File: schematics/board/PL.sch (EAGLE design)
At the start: 28 parts, among them IC2 STM32F103C8T, Q5 8MHz

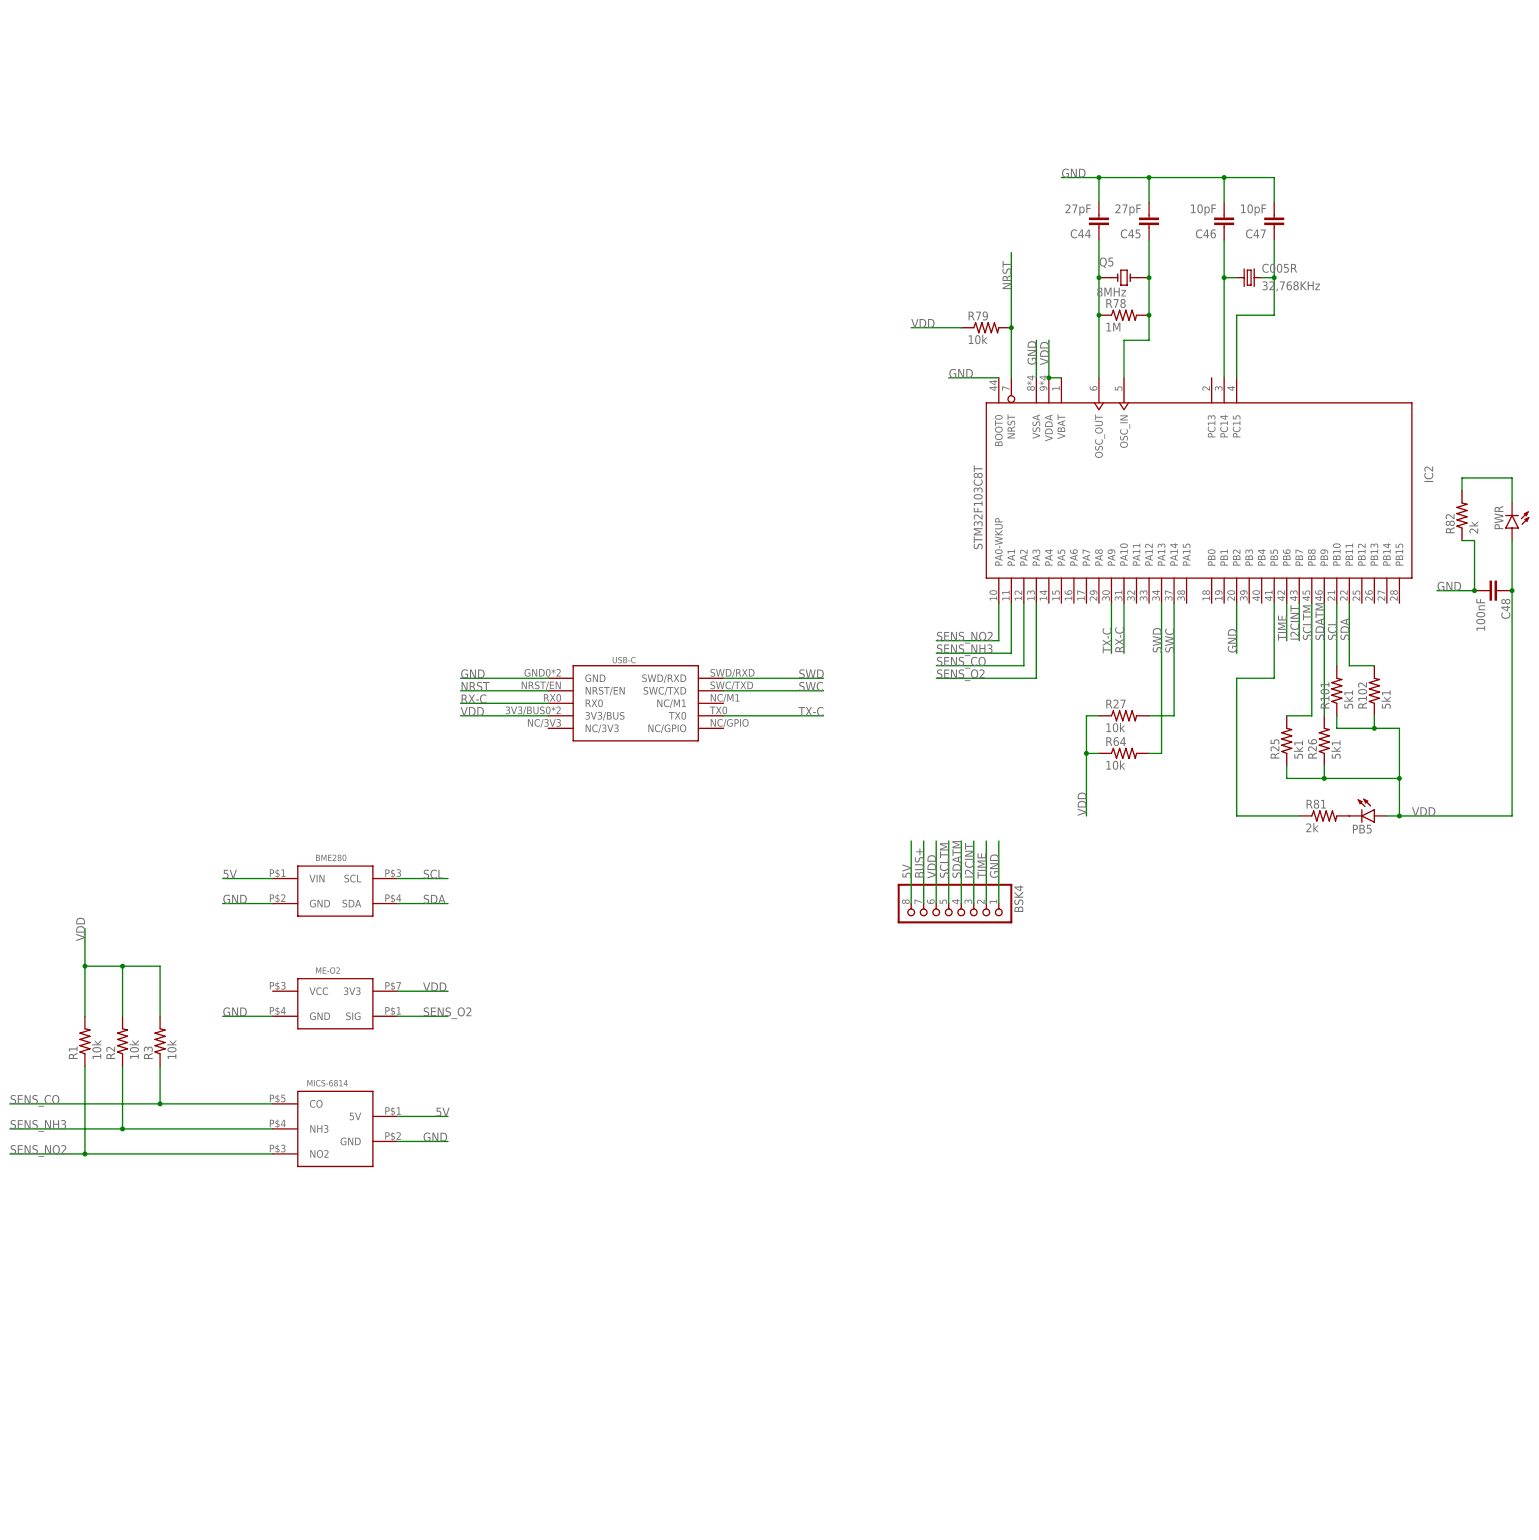
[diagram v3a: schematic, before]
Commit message: На плату полезной нагрузки добавлены управляемые резисторы для управления балансирующими сопротивлениями для газового датчика
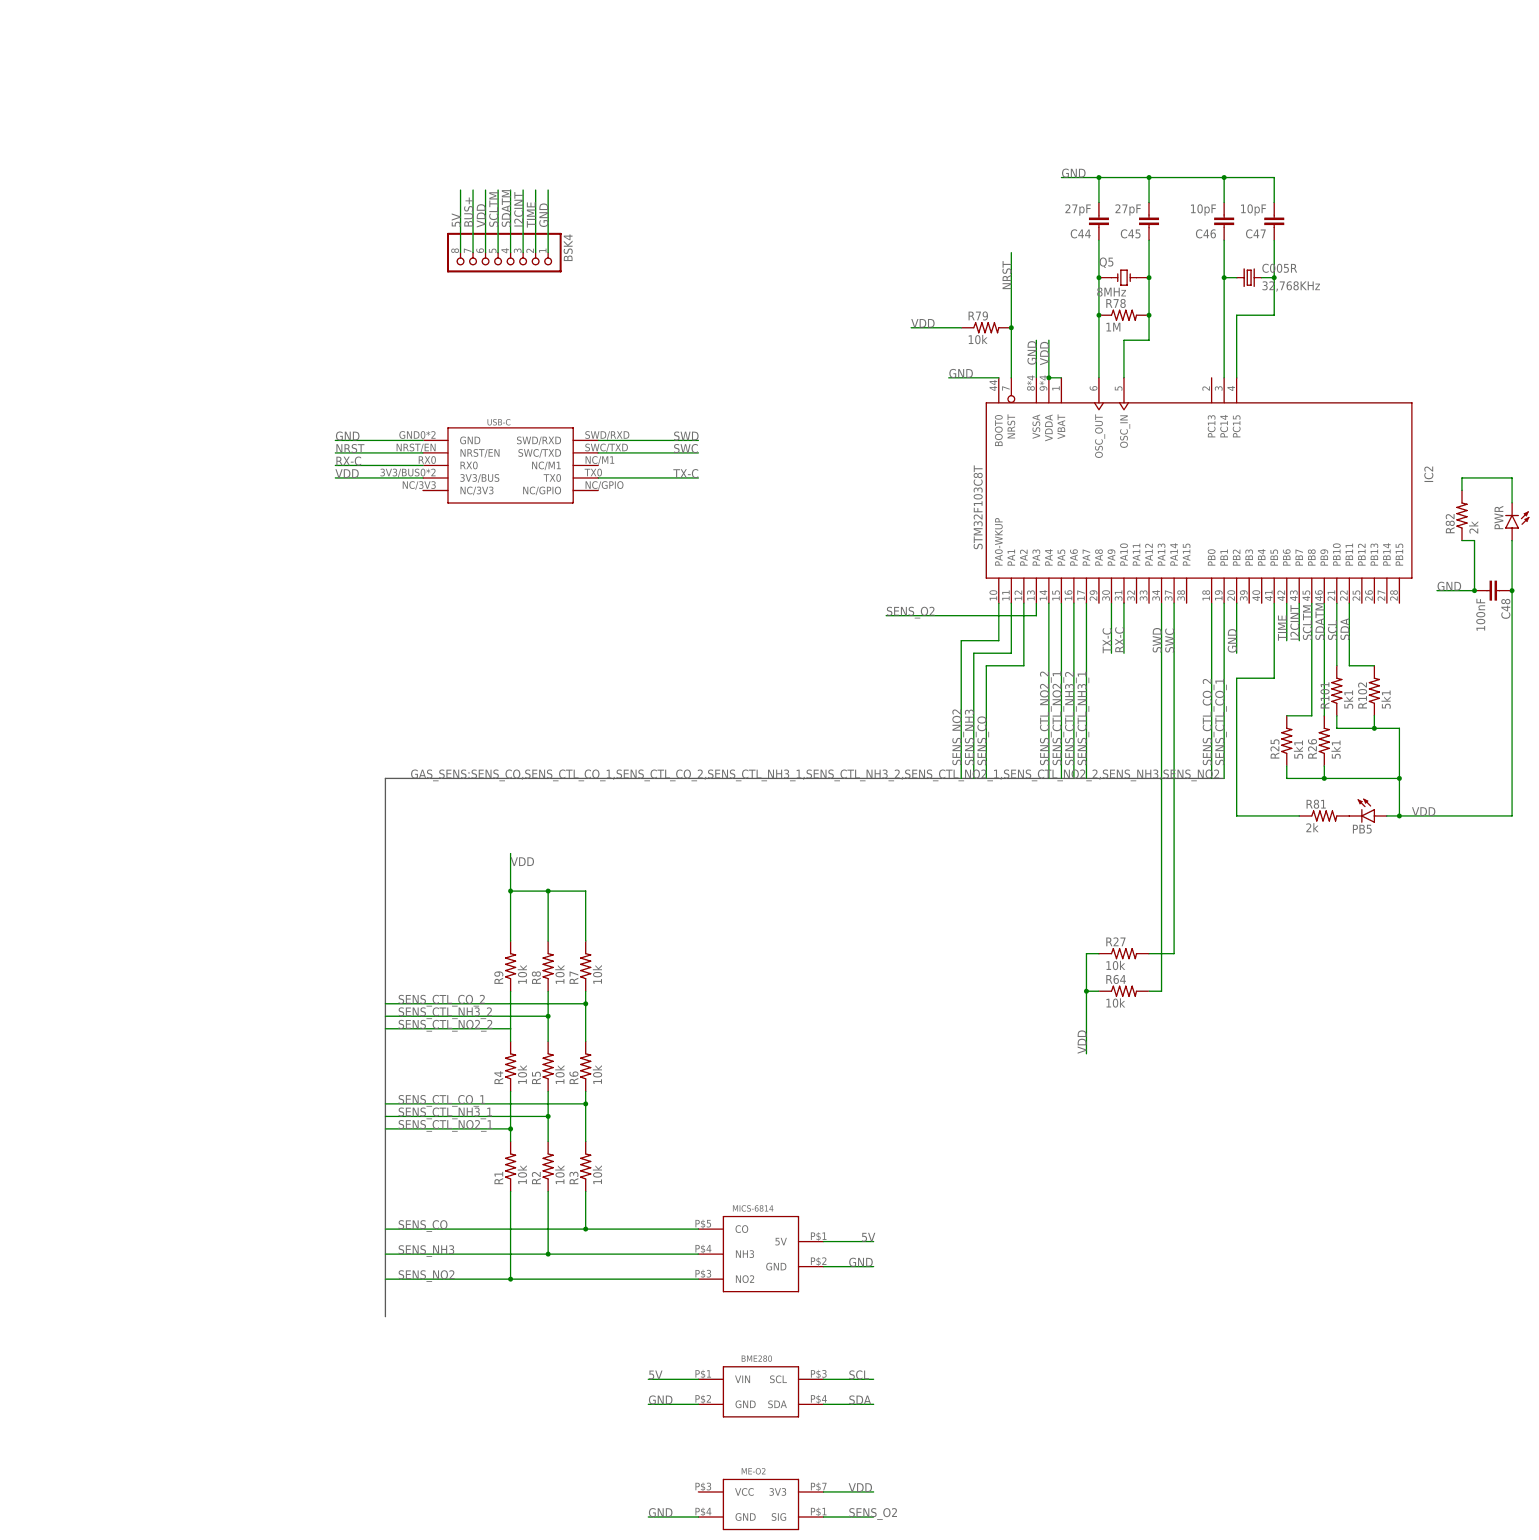
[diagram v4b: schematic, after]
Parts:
- added R4, R5, R6, R7, R8, R9: 10k, resistor:R-US_R0603
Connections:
- new net SENS_CTL_CO_1: IC2.PB1, R3.2, R6.1
- new net SENS_CTL_CO_2: IC2.PB0, R6.2, R7.1
- new net SENS_CTL_NH3_1: IC2.PA7, R2.2, R5.1
- new net SENS_CTL_NH3_2: IC2.PA6, R5.2, R8.1
- new net SENS_CTL_NO2_1: IC2.PA5, R1.2, R4.1
- new net SENS_CTL_NO2_2: IC2.PA4, R4.2, R9.1
- net VDD: now also R7.2, R8.2, R9.2; no longer R1.2, R2.2, R3.2
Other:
- moved on the sheet: BME280, BSK4, ME-O2, MICS-6814, R1, R2, R27, R3, R64

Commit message: Изменения в подключении мк
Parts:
- added C15, C53, C54, C55: 100nF, rcl:C-EUC0603
- added C16: 10µ, rcl:C-USC1206
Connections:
- net GND: now also C15.2, C16.2, C53.2, C54.2, C55.2
- net VDD: now also C15.1, C16.1, C53.1, C54.1, C55.1
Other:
- moved on the sheet: R79
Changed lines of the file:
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@@
 <?xml version="1.0" encoding="utf-8"?>
 <!DOCTYPE eagle SYSTEM "eagle.dtd">
-<eagle version="9.6.0">
+<eagle version="9.4.2">
 <drawing>
 <settings>
@@
 <part name="R8" library="resistor" library_urn="urn:adsk.eagle:library:348" deviceset="R-US_" device="R0603" package3d_urn="urn:adsk.eagle:package:23555/3" value="10k"/>
 <part name="R9" library="resistor" library_urn="urn:adsk.eagle:library:348" deviceset="R-US_" device="R0603" package3d_urn="urn:adsk.eagle:package:23555/3" value="10k"/>
+<part name="C15" library="rcl" library_urn="urn:adsk.eagle:library:334" deviceset="C-EU" device="C0603" package3d_urn="urn:adsk.eagle:package:23616/2" value="100nF"/>
+<part name="C16" library="rcl" library_urn="urn:adsk.eagle:library:334" deviceset="C-US" device="C1206" package3d_urn="urn:adsk.eagle:package:23618/2" value="10µ"/>
+<part name="C53" library="rcl" library_urn="urn:adsk.eagle:library:334" deviceset="C-EU" device="C0603" package3d_urn="urn:adsk.eagle:package:23616/2" value="100nF"/>
+<part name="C54" library="rcl" library_urn="urn:adsk.eagle:library:334" deviceset="C-EU" device="C0603" package3d_urn="urn:adsk.eagle:package:23616/2" value="100nF"/>
+<part name="C55" library="rcl" library_urn="urn:adsk.eagle:library:334" deviceset="C-EU" device="C0603" package3d_urn="urn:adsk.eagle:package:23616/2" value="100nF"/>
 </parts>
 <sheets>
@@
 <attribute name="VALUE" x="139.7" y="152.4" size="1.778" layer="96"/>
 </instance>
-<instance part="R79" gate="G$1" x="83.82" y="144.78" smashed="yes">
-<attribute name="NAME" x="80.01" y="146.2786" size="1.778" layer="95"/>
-<attribute name="VALUE" x="80.01" y="141.478" size="1.778" layer="96"/>
+<instance part="R79" gate="G$1" x="66.04" y="147.32" smashed="yes">
+<attribute name="NAME" x="62.23" y="148.8186" size="1.778" layer="95"/>
+<attribute name="VALUE" x="62.23" y="144.018" size="1.778" layer="96"/>
 </instance>
 <instance part="R101" gate="G$1" x="154.94" y="71.12" smashed="yes" rot="R90">
@@
 <attribute name="NAME" x="-14.1986" y="11.43" size="1.778" layer="95" rot="R90"/>
 <attribute name="VALUE" x="-9.398" y="11.43" size="1.778" layer="96" rot="R90"/>
+</instance>
+<instance part="C15" gate="G$1" x="93.98" y="160.02" smashed="yes" rot="R270">
+<attribute name="NAME" x="94.361" y="158.496" size="1.778" layer="95" rot="R270"/>
+<attribute name="VALUE" x="89.281" y="158.496" size="1.778" layer="96" rot="R270"/>
+</instance>
+<instance part="C16" gate="G$1" x="93.98" y="165.1" smashed="yes" rot="R270">
+<attribute name="NAME" x="94.615" y="164.084" size="1.778" layer="95" rot="R270"/>
+<attribute name="VALUE" x="89.789" y="164.084" size="1.778" layer="96" rot="R270"/>
+</instance>
+<instance part="C53" gate="G$1" x="93.98" y="172.72" smashed="yes" rot="R270">
+<attribute name="NAME" x="94.361" y="171.196" size="1.778" layer="95" rot="R270"/>
+<attribute name="VALUE" x="89.281" y="171.196" size="1.778" layer="96" rot="R270"/>
+</instance>
+<instance part="C54" gate="G$1" x="93.98" y="180.34" smashed="yes" rot="R270">
+<attribute name="NAME" x="94.361" y="178.816" size="1.778" layer="95" rot="R270"/>
+<attribute name="VALUE" x="89.281" y="178.816" size="1.778" layer="96" rot="R270"/>
+</instance>
+<instance part="C55" gate="G$1" x="93.98" y="187.96" smashed="yes" rot="R270">
+<attribute name="NAME" x="94.361" y="186.436" size="1.778" layer="95" rot="R270"/>
+<attribute name="VALUE" x="89.281" y="186.436" size="1.778" layer="96" rot="R270"/>
 </instance>
 </instances>
@@
 </segment>
 <segment>
-<wire x1="93.98" y1="134.62" x2="93.98" y2="142.24" width="0.1524" layer="91"/>
-<label x="93.98" y="137.16" size="1.778" layer="95" rot="R90"/>
+<wire x1="93.98" y1="134.62" x2="93.98" y2="149.86" width="0.1524" layer="91"/>
+<label x="88.9" y="203.2" size="1.778" layer="95" rot="R90"/>
 <pinref part="IC2" gate="MCU" pin="VSSA"/>
+<wire x1="93.98" y1="149.86" x2="88.9" y2="149.86" width="0.1524" layer="91"/>
+<wire x1="88.9" y1="149.86" x2="88.9" y2="160.02" width="0.1524" layer="91"/>
+<pinref part="C15" gate="G$1" pin="2"/>
+<wire x1="88.9" y1="160.02" x2="88.9" y2="165.1" width="0.1524" layer="91"/>
+<junction x="88.9" y="160.02"/>
+<pinref part="C16" gate="G$1" pin="2"/>
+<wire x1="88.9" y1="165.1" x2="88.9" y2="172.72" width="0.1524" layer="91"/>
+<junction x="88.9" y="165.1"/>
+<pinref part="C53" gate="G$1" pin="2"/>
+<wire x1="88.9" y1="172.72" x2="88.9" y2="180.34" width="0.1524" layer="91"/>
+<junction x="88.9" y="172.72"/>
+<pinref part="C54" gate="G$1" pin="2"/>
+<wire x1="88.9" y1="180.34" x2="88.9" y2="187.96" width="0.1524" layer="91"/>
+<junction x="88.9" y="180.34"/>
+<pinref part="C55" gate="G$1" pin="2"/>
+<wire x1="88.9" y1="187.96" x2="88.9" y2="208.28" width="0.1524" layer="91"/>
+<junction x="88.9" y="187.96"/>
 </segment>
 <segment>
@@
 </segment>
 <segment>
-<wire x1="96.52" y1="134.62" x2="96.52" y2="142.24" width="0.1524" layer="91"/>
-<label x="96.52" y="137.16" size="1.778" layer="95" rot="R90"/>
+<wire x1="96.52" y1="134.62" x2="96.52" y2="160.02" width="0.1524" layer="91"/>
+<label x="96.52" y="203.2" size="1.778" layer="95" rot="R90"/>
 <pinref part="IC2" gate="MCU" pin="VDDA"/>
 <pinref part="IC2" gate="MCU" pin="VBAT"/>
+<wire x1="96.52" y1="160.02" x2="96.52" y2="165.1" width="0.1524" layer="91"/>
+<wire x1="96.52" y1="165.1" x2="96.52" y2="172.72" width="0.1524" layer="91"/>
+<wire x1="96.52" y1="172.72" x2="96.52" y2="180.34" width="0.1524" layer="91"/>
+<wire x1="96.52" y1="180.34" x2="96.52" y2="187.96" width="0.1524" layer="91"/>
+<wire x1="96.52" y1="187.96" x2="96.52" y2="208.28" width="0.1524" layer="91"/>
 <wire x1="99.06" y1="134.62" x2="96.52" y2="134.62" width="0.1524" layer="91"/>
 <junction x="96.52" y="134.62"/>
+<pinref part="C15" gate="G$1" pin="1"/>
+<junction x="96.52" y="160.02"/>
+<pinref part="C16" gate="G$1" pin="1"/>
+<junction x="96.52" y="165.1"/>
+<pinref part="C53" gate="G$1" pin="1"/>
+<junction x="96.52" y="172.72"/>
+<pinref part="C54" gate="G$1" pin="1"/>
+<junction x="96.52" y="180.34"/>
+<pinref part="C55" gate="G$1" pin="1"/>
+<junction x="96.52" y="187.96"/>
 </segment>
 <segment>
@@
 </segment>
 <segment>
-<wire x1="78.74" y1="144.78" x2="68.58" y2="144.78" width="0.1524" layer="91"/>
-<label x="68.58" y="144.78" size="1.778" layer="95"/>
+<wire x1="60.96" y1="147.32" x2="50.8" y2="147.32" width="0.1524" layer="91"/>
+<label x="50.8" y="147.32" size="1.778" layer="95"/>
 <pinref part="R79" gate="G$1" pin="1"/>
 </segment>
@@
 <net name="NRST" class="0">
 <segment>
-<wire x1="88.9" y1="134.62" x2="88.9" y2="144.78" width="0.1524" layer="91"/>
-<wire x1="88.9" y1="144.78" x2="88.9" y2="160.02" width="0.1524" layer="91"/>
-<junction x="88.9" y="144.78"/>
-<label x="88.9" y="152.4" size="1.778" layer="95" rot="R90"/>
+<wire x1="71.12" y1="147.32" x2="71.12" y2="162.56" width="0.1524" layer="91"/>
+<junction x="71.12" y="147.32"/>
+<label x="71.12" y="154.94" size="1.778" layer="95" rot="R90"/>
 <pinref part="R79" gate="G$1" pin="2"/>
 <pinref part="IC2" gate="MCU" pin="NRST"/>
-</segment>
-<segment>
+<wire x1="88.9" y1="134.62" x2="88.9" y2="147.32" width="0.1524" layer="91"/>
+<wire x1="88.9" y1="147.32" x2="71.12" y2="147.32" width="0.1524" layer="91"/>
+</segment>
+<segment>
